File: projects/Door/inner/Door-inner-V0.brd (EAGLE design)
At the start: 80 x 53.3 mm, 28 parts, among them IC1 7815TV, J2 AVR_SPI_PROG_3X2PTH, J3 LCD, U2 LP2985-33DBVR, X1 POWERSUPPLY_DC21MMX, Y1 16MHz

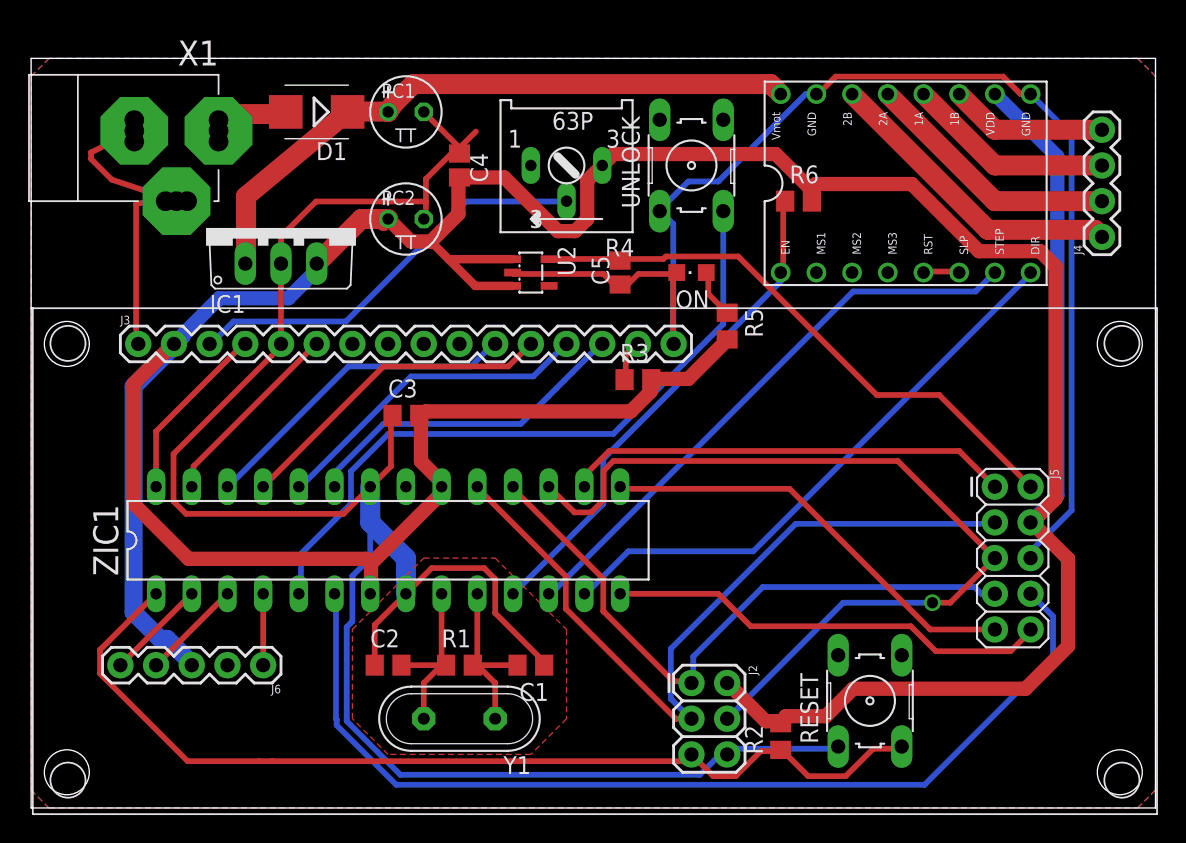
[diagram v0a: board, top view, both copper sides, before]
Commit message: Door-inner redesign
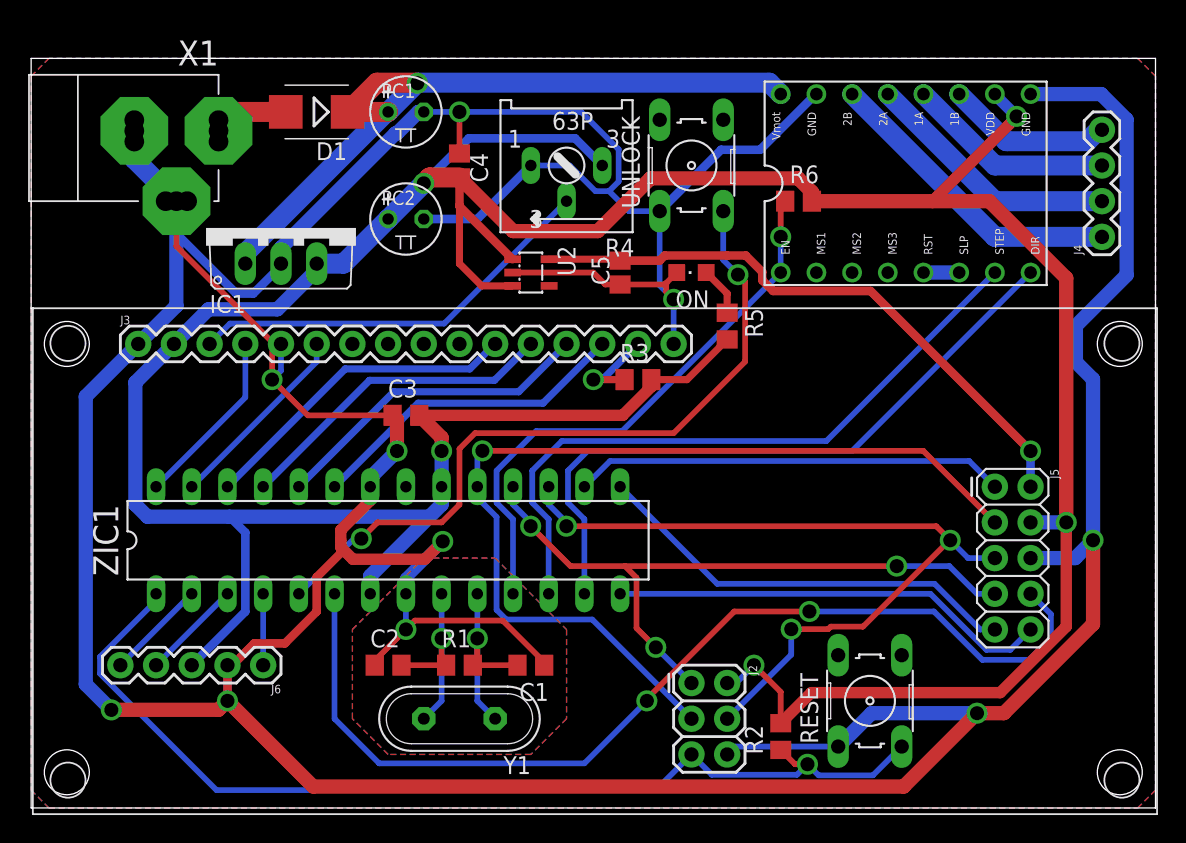
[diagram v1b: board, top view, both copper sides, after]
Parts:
- J3: value LCD -> LCD_4PIN
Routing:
- net GND: track 266.4 -> 387.9 mm, vias 0 -> 10
- net +5V: track 280.7 -> 260.8 mm, vias 0 -> 5
- net SCK: track 55.9 -> 67.7 mm, vias 0 -> 1
- net MOSI: track 64.0 -> 57.0 mm, vias 1 -> 3
- net M-STP: track 41.2 -> 48.0 mm
- net M-DIR: track 41.3 -> 48.0 mm
- net VIN: track 46.2 -> 52.9 mm, vias 0 -> 1
- net M-EN: track 36.0 -> 40.5 mm, vias 0 -> 1
- net N$4: track 3.29 -> 6.45 mm, vias 0 -> 1
- net N$12: track 49.2 -> 52.3 mm, vias 0 -> 2
- net MISO: track 45.6 -> 48.6 mm, vias 0 -> 3
- net RESET: track 70.3 -> 73.3 mm, vias 0 -> 1
- net XTAL2: track 12.7 -> 14.6 mm, vias 0 -> 1
- net XTAL1: track 12.7 -> 14.6 mm, vias 0 -> 1
- net +3V3: track 41.3 -> 43.1 mm, vias 0 -> 1
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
